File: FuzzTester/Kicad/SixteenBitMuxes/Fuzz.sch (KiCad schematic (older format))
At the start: 11 parts, among them J2 POT B10K JST XH, J3 POT B5K JST XH, J4 VOL POT A100K JST XH

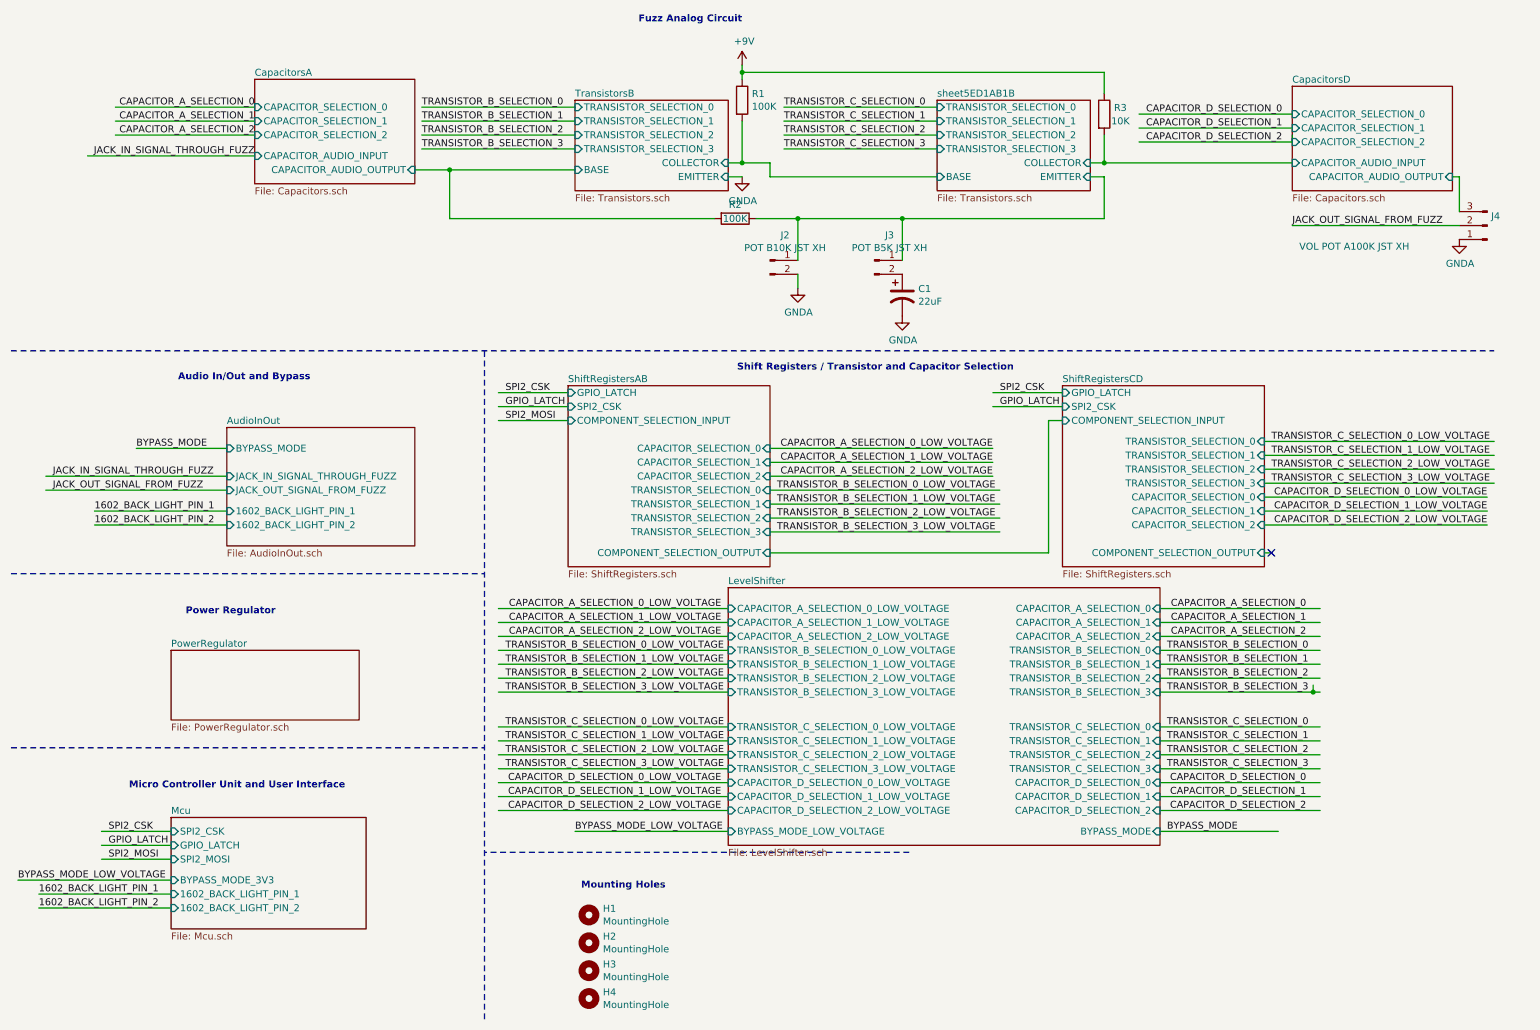
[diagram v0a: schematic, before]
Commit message: Removed shift registers
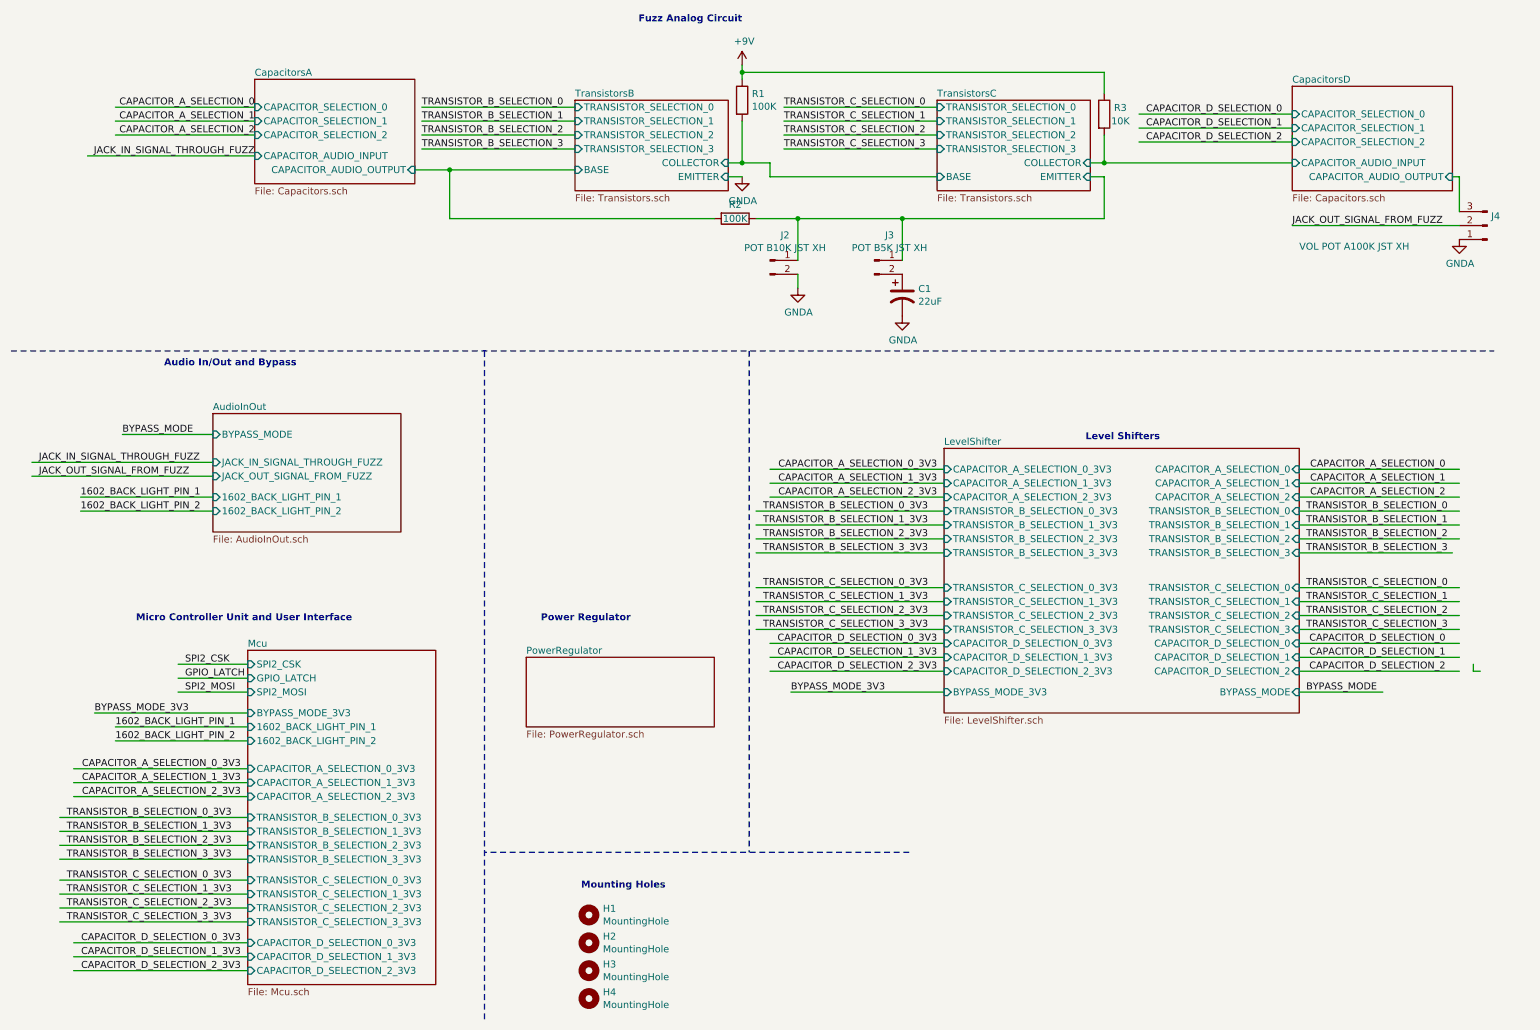
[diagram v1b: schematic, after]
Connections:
- net labels added: BYPASS_MODE_3V3, CAPACITOR_A_SELECTION_0_3V3, CAPACITOR_A_SELECTION_1_3V3, CAPACITOR_A_SELECTION_2_3V3, CAPACITOR_D_SELECTION_0_3V3, CAPACITOR_D_SELECTION_1_3V3, CAPACITOR_D_SELECTION_2_3V3, TRANSISTOR_B_SELECTION_0_3V3, TRANSISTOR_B_SELECTION_1_3V3, TRANSISTOR_B_SELECTION_2_3V3, TRANSISTOR_B_SELECTION_3_3V3, TRANSISTOR_C_SELECTION_0_3V3, TRANSISTOR_C_SELECTION_1_3V3, TRANSISTOR_C_SELECTION_2_3V3, TRANSISTOR_C_SELECTION_3_3V3
- net labels removed: BYPASS_MODE_LOW_VOLTAGE, CAPACITOR_A_SELECTION_0_LOW_VOLTAGE, CAPACITOR_A_SELECTION_1_LOW_VOLTAGE, CAPACITOR_A_SELECTION_2_LOW_VOLTAGE, CAPACITOR_D_SELECTION_0_LOW_VOLTAGE, CAPACITOR_D_SELECTION_1_LOW_VOLTAGE, CAPACITOR_D_SELECTION_2_LOW_VOLTAGE, TRANSISTOR_B_SELECTION_0_LOW_VOLTAGE, TRANSISTOR_B_SELECTION_1_LOW_VOLTAGE, TRANSISTOR_B_SELECTION_2_LOW_VOLTAGE, TRANSISTOR_B_SELECTION_3_LOW_VOLTAGE, TRANSISTOR_C_SELECTION_0_LOW_VOLTAGE, TRANSISTOR_C_SELECTION_1_LOW_VOLTAGE, TRANSISTOR_C_SELECTION_2_LOW_VOLTAGE, TRANSISTOR_C_SELECTION_3_LOW_VOLTAGE
- wire segments 110 -> 101
- no-connect marks 1 -> 0
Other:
- note added: "Level Shifters\n"
- note removed: "Shift Registers / Transistor and Capacitor Selection\n"

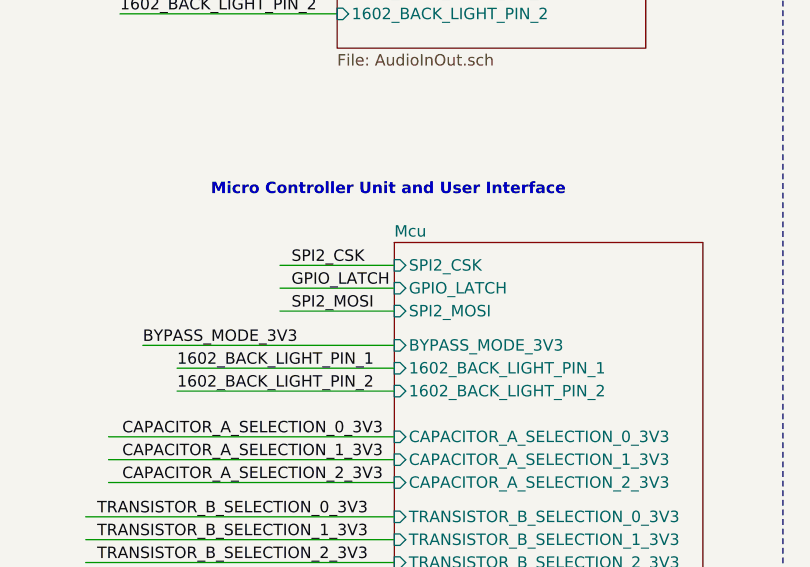
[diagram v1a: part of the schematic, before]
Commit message: Finished (but not beautiful) PCB without SPI and most 8 channel multiplexers.
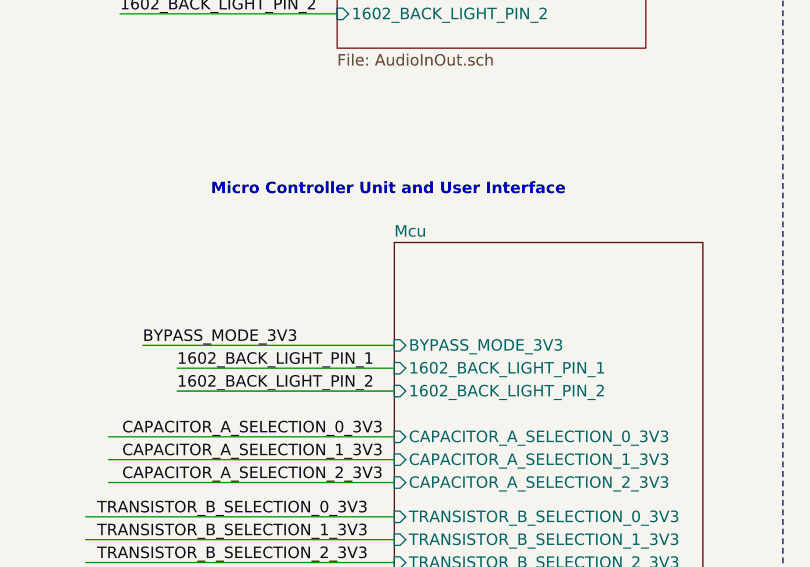
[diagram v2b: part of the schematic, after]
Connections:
- net labels removed: GPIO_LATCH, SPI2_CSK, SPI2_MOSI
- wire segments 101 -> 98
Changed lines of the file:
@@
 Text Label 2250 1400 2    50   ~ 0
 CAPACITOR_A_SELECTION_2
-Text Label 1750 5200 0    50   ~ 0
-SPI2_CSK
-Text Label 1750 5300 0    50   ~ 0
-GPIO_LATCH
-Wire Wire Line
-	1700 5400 2200 5400
-Text Label 1750 5400 0    50   ~ 0
-SPI2_MOSI
-Wire Wire Line
-	1700 5300 2200 5300
-Wire Wire Line
-	1700 5200 2200 5200
 Wire Wire Line
 	3400 1650 3650 1650
@@
 Wire Wire Line
 	650  3750 1950 3750
-$Sheet
-S 2200 5100 1350 2400
-U 5E8BDF21
-F0 "Mcu" 50
-F1 "Mcu.sch" 50
-F2 "GPIO_LATCH" I L 2200 5300 50
-F3 "SPI2_CSK" I L 2200 5200 50
-F4 "SPI2_MOSI" I L 2200 5400 50
-F5 "1602_BACK_LIGHT_PIN_1" I L 2200 5650 50
-F6 "1602_BACK_LIGHT_PIN_2" I L 2200 5750 50
-F7 "BYPASS_MODE_3V3" I L 2200 5550 50
-F8 "TRANSISTOR_B_SELECTION_0_3V3" I L 2200 6300 50
-F9 "TRANSISTOR_B_SELECTION_1_3V3" I L 2200 6400 50
-F10 "TRANSISTOR_B_SELECTION_2_3V3" I L 2200 6500 50
-F11 "TRANSISTOR_B_SELECTION_3_3V3" I L 2200 6600 50
-F12 "CAPACITOR_A_SELECTION_0_3V3" I L 2200 5950 50
-F13 "CAPACITOR_A_SELECTION_1_3V3" I L 2200 6050 50
-F14 "CAPACITOR_A_SELECTION_2_3V3" I L 2200 6150 50
-F15 "TRANSISTOR_C_SELECTION_0_3V3" I L 2200 6750 50
-F16 "TRANSISTOR_C_SELECTION_1_3V3" I L 2200 6850 50
-F17 "TRANSISTOR_C_SELECTION_2_3V3" I L 2200 6950 50
-F18 "TRANSISTOR_C_SELECTION_3_3V3" I L 2200 7050 50
-F19 "CAPACITOR_D_SELECTION_0_3V3" I L 2200 7200 50
-F20 "CAPACITOR_D_SELECTION_1_3V3" I L 2200 7300 50
-F21 "CAPACITOR_D_SELECTION_2_3V3" I L 2200 7400 50
-$EndSheet
 $Comp
 L power:GNDA #PWR03
@@
 Wire Wire Line
 	950  7400 2200 7400
+$Sheet
+S 2200 5100 1350 2400
+U 5E8BDF21
+F0 "Mcu" 50
+F1 "Mcu.sch" 50
+F2 "1602_BACK_LIGHT_PIN_1" I L 2200 5650 50
+F3 "1602_BACK_LIGHT_PIN_2" I L 2200 5750 50
+F4 "BYPASS_MODE_3V3" I L 2200 5550 50
+F5 "TRANSISTOR_B_SELECTION_0_3V3" I L 2200 6300 50
+F6 "TRANSISTOR_B_SELECTION_1_3V3" I L 2200 6400 50
+F7 "TRANSISTOR_B_SELECTION_2_3V3" I L 2200 6500 50
+F8 "TRANSISTOR_B_SELECTION_3_3V3" I L 2200 6600 50
+F9 "CAPACITOR_A_SELECTION_0_3V3" I L 2200 5950 50
+F10 "CAPACITOR_A_SELECTION_1_3V3" I L 2200 6050 50
+F11 "CAPACITOR_A_SELECTION_2_3V3" I L 2200 6150 50
+F12 "TRANSISTOR_C_SELECTION_0_3V3" I L 2200 6750 50
+F13 "TRANSISTOR_C_SELECTION_1_3V3" I L 2200 6850 50
+F14 "TRANSISTOR_C_SELECTION_2_3V3" I L 2200 6950 50
+F15 "TRANSISTOR_C_SELECTION_3_3V3" I L 2200 7050 50
+F16 "CAPACITOR_D_SELECTION_0_3V3" I L 2200 7200 50
+F17 "CAPACITOR_D_SELECTION_1_3V3" I L 2200 7300 50
+F18 "CAPACITOR_D_SELECTION_2_3V3" I L 2200 7400 50
+$EndSheet
 $EndSCHEMATC
